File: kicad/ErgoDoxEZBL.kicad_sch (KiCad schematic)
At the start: 79 parts, among them J1 Barrel_Jack, SW0:0 SW_Push, SW0:1 SW_Push, SW0:2 SW_Push, SW0:3 SW_Push, SW0:4 SW_Push, SW0:5 SW_Push, SW1 SW_DPST_x2, SW1:2 SW_Push, SW1:3 SW_Push, SW1:4 SW_Push, SW1:5 SW_Push, SW1:6 SW_Push, SW2:0 SW_Push, SW2:1 SW_Push, SW2:2 SW_Push, SW2:3 SW_Push, SW2:4 SW_Push, SW2:5 SW_Push, SW2:6 SW_Push, SW3:1 SW_Push, SW3:2 SW_Push, SW3:3 SW_Push, SW3:4 SW_Push, SW3:5 SW_Push, SW3:6 SW_Push, SW4:0 SW_Push, SW4:1 SW_Push, SW4:2 SW_Push, SW4:3 SW_Push, SW4:4 SW_Push, SW4:5 SW_Push, SW4:6 SW_Push, SW5:0 SW_Push, SW5:1 SW_Push, SW5:2 SW_Push, SW5:3 SW_Push, SW5:4 SW_Push, SW5:5 SW_Push

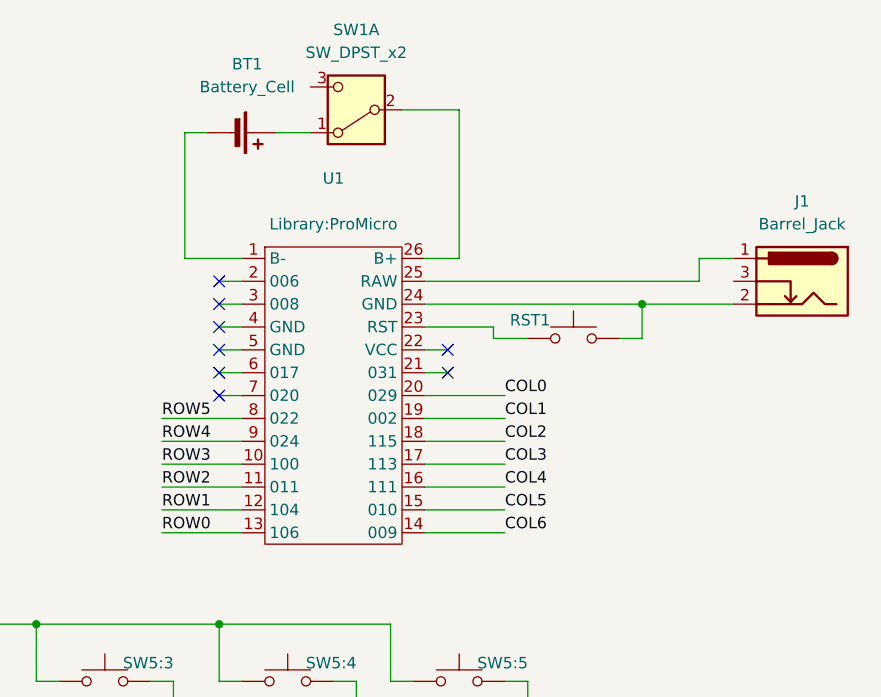
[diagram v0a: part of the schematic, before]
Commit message: PCB v2
- Fix DC jack footprint
- Single reversible PCB for both split
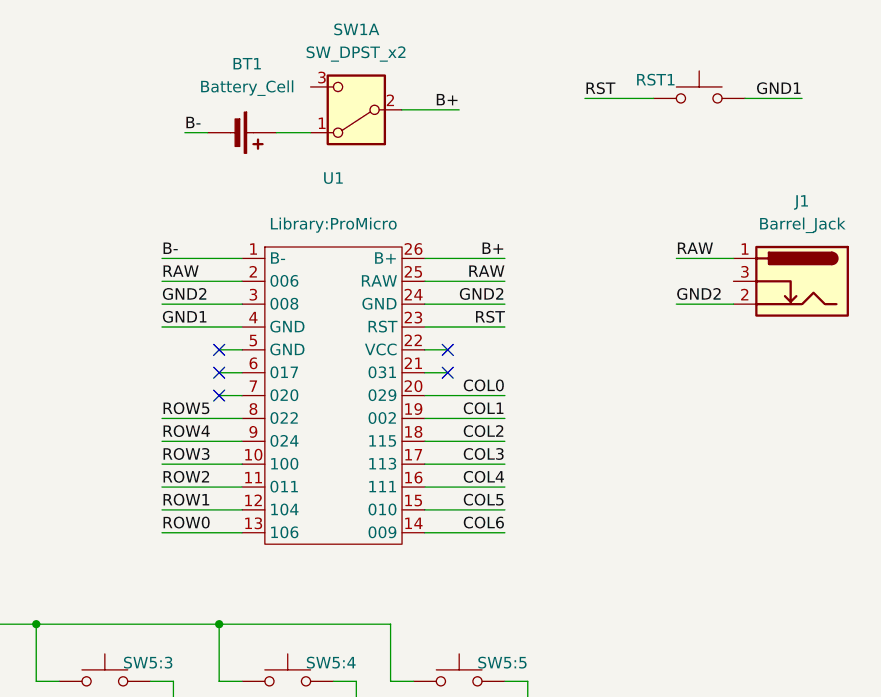
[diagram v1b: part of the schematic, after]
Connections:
- net B-: now reaches BT1.2 (-), U1.1 (B-)
- net RAW: now reaches J1.1 (PWR), U1.25 (RAW)
- net RAW: now also U1.2 (006)
- net GND2: now reaches J1.2 (GND), U1.24 (GND)
- net GND2: now also U1.3 (008); no longer RST1.1
- net RST: now reaches RST1.2, U1.23 (RST)
- net B+: now reaches SW1.2 (B), U1.26 (B+)
- net GND1: now reaches U1.4 (GND)
- net GND1: now also RST1.1
- no-connect marks 8 -> 5
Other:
- title: Ergo Dox BL - right hand -> ErgoDox EZBL
- moved on the sheet: RST1

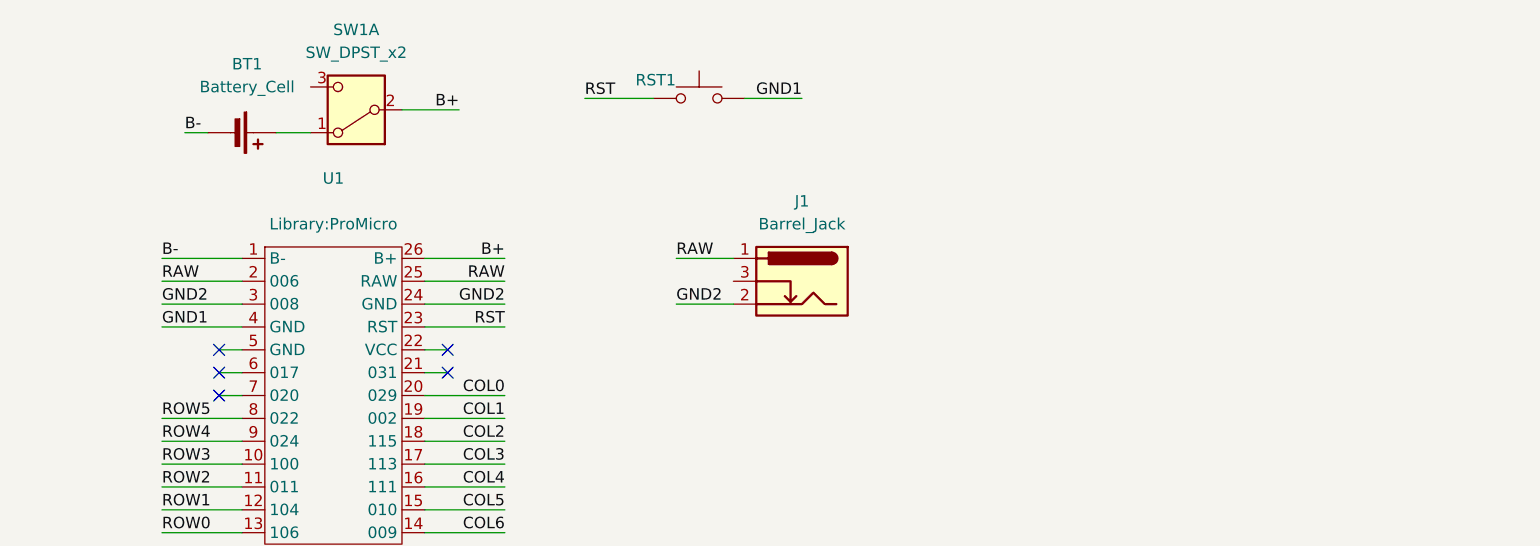
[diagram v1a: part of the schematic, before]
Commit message: USB connection via TRRS jack connector
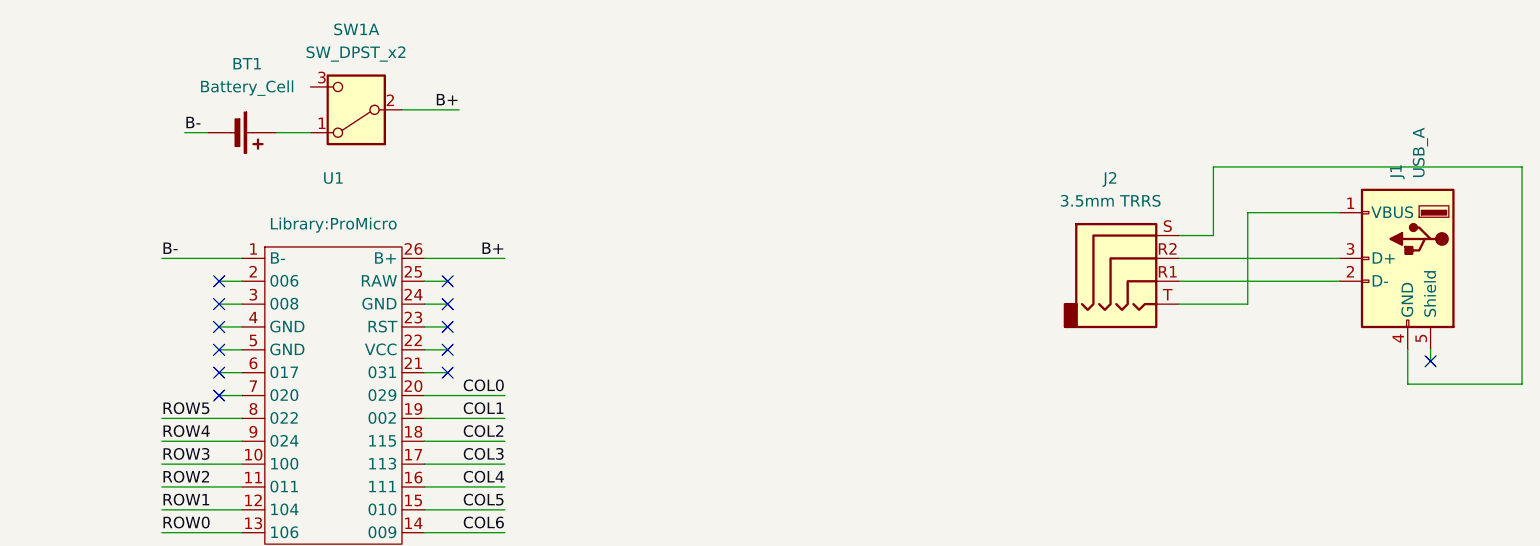
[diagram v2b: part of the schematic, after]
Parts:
- removed J1: Barrel_Jack, Library:DC-033, symbol PCM_SparkFun-Connector:Barrel_Jack_PTH
- removed RST1: SW_Push, Library:Push button, symbol Switch:SW_Push
- added J1: USB_A, Connector_Wire:SolderWire-0.1sqmm_1x04_P3.6mm_D0.4mm_OD1mm, symbol Connector:USB_A
- added J2: 3.5mm TRRS, Library:SJ3-35094A, symbol PCM_SparkFun-Connector:Audio_Jack_TRRS_3.5mm_SMD
- U1: value ~ -> (none)
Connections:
- net GND1: no longer names the net of U1.4 (GND)
- net GND2: no longer names the net of U1.24 (GND)
- net GND2: no longer U1.3 (008)
- net RAW: no longer names the net of U1.2 (006)
- net RAW: no longer U1.25 (RAW)
- net RST: no longer names the net of U1.23 (RST)
- new net: J1.2 (D-), J2.R1
- new net: J1.3 (D+), J2.R2
- new net: J1.4 (GND), J2.S
- new net: J1.1 (VBUS), J2.T
- no-connect marks 5 -> 12
